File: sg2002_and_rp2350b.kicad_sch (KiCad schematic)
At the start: 33 parts, among them J2 Conn_01x14, J3 Conn_01x14, U10 W25Q128JVSIQTR, X3 12MHz

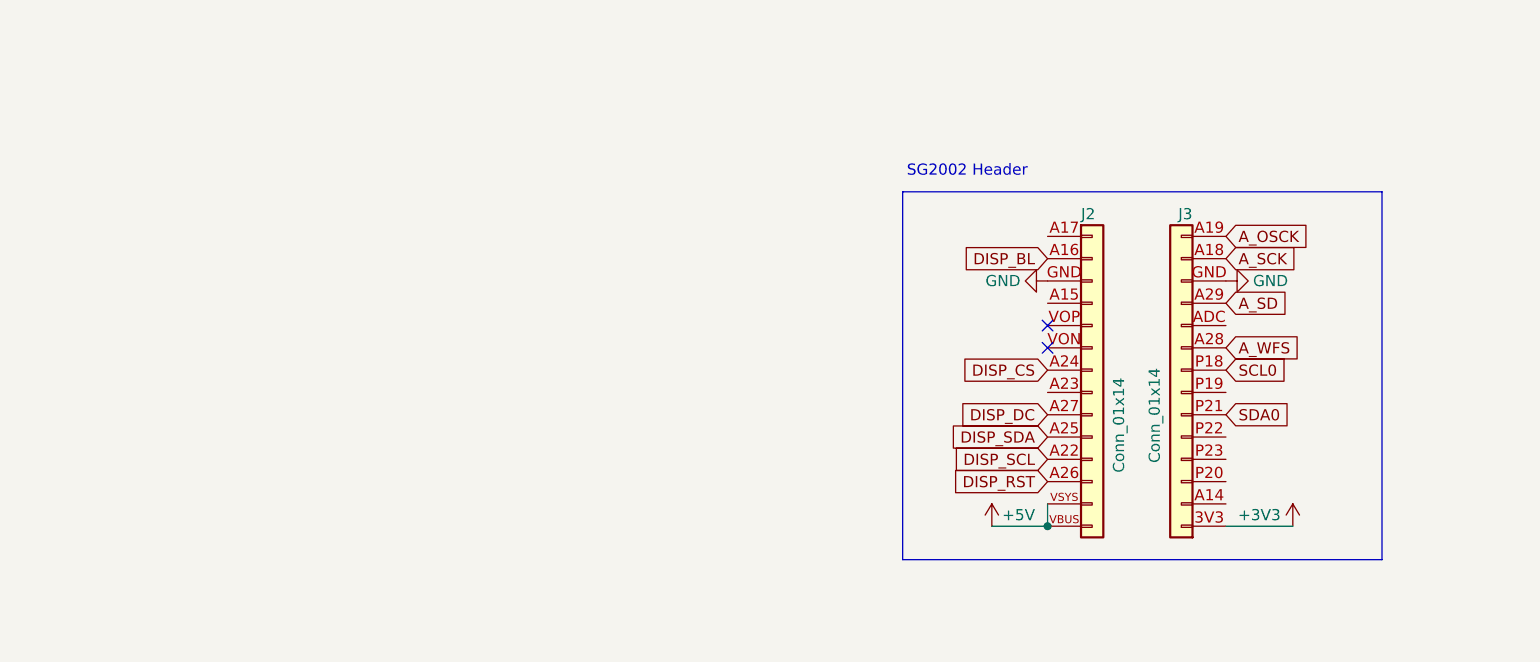
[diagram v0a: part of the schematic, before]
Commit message: Changed to touchscreen LCD and added connectors for front breakout
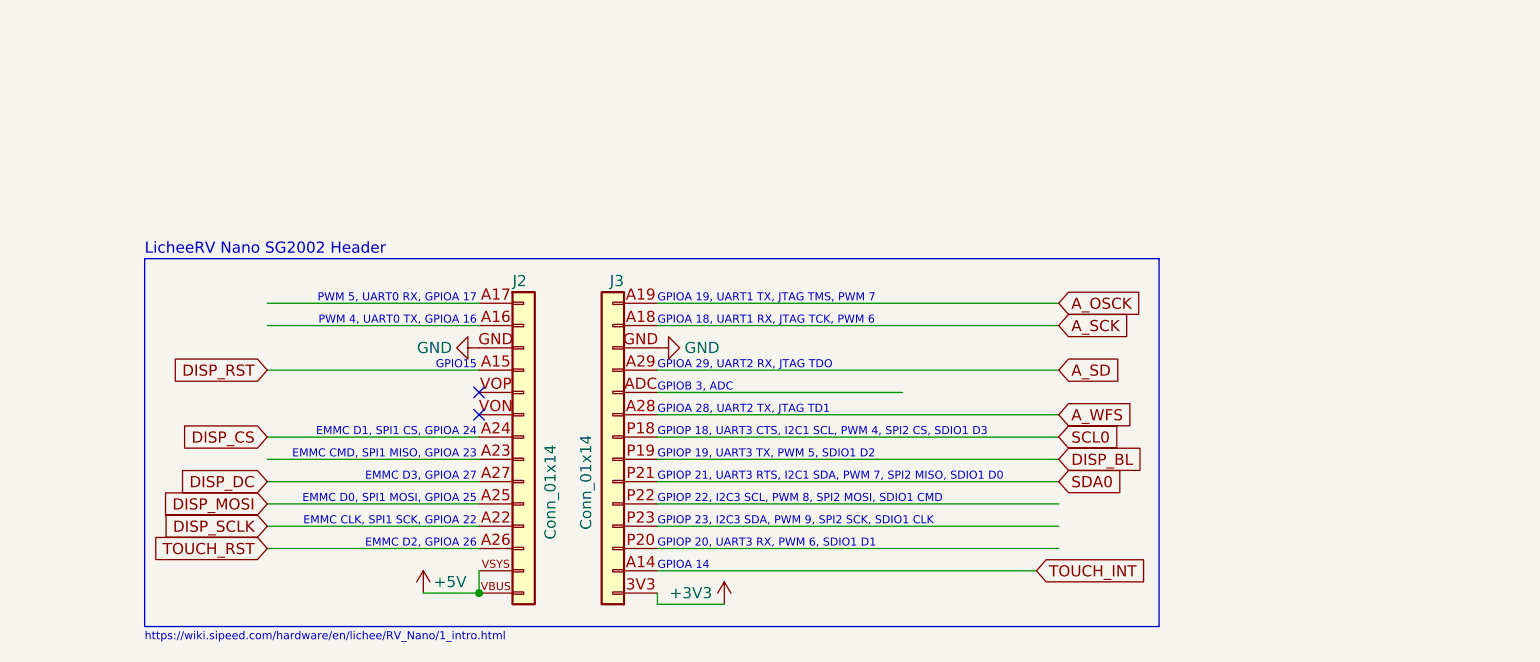
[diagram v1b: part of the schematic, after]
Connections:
- net DISP_BL: now also J3.P19 (Pin_7); no longer J2.A16 (Pin_2)
- net DISP_RST: now also J2.A15 (Pin_4); no longer J2.A26 (Pin_12)
- net TOUCH_INT: now reaches J3.A14 (Pin_2)
- net DISP_SCL renamed DISP_SCLK
- net DISP_SDA renamed DISP_MOSI
- new net TOUCH_RST: J2.A26 (Pin_12)
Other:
- note added: "EMMC CLK, SPI1 SCK, GPIOA 22"
- note added: "EMMC CMD, SPI1 MISO, GPIOA 23"
- note added: "EMMC D0, SPI1 MOSI, GPIOA 25"
- note added: "EMMC D1, SPI1 CS, GPIOA 24"
- note added: "EMMC D2, GPIOA 26"
- note added: "EMMC D3, GPIOA 27"
- note added: "GPIO15"
- note added: "GPIOA 14"
- note added: "GPIOA 18, UART1 RX, JTAG TCK, PWM 6"
- note added: "GPIOA 19, UART1 TX, JTAG TMS, PWM 7"
- note added: "GPIOA 28, UART2 TX, JTAG TD1"
- note added: "GPIOA 29, UART2 RX, JTAG TDO"
- note added: "GPIOB 3, ADC"
- note added: "GPIOP 18, UART3 CTS, I2C1 SCL, PWM 4, SPI2 CS, SDIO1 D3"
- note added: "GPIOP 19, UART3 TX, PWM 5, SDIO1 D2"
- note added: "GPIOP 20, UART3 RX, PWM 6, SDIO1 D1"
- note added: "GPIOP 21, UART3 RTS, I2C1 SDA, PWM 7, SPI2 MISO, SDIO1 D0"
- note added: "GPIOP 22, I2C3 SCL, PWM 8, SPI2 MOSI, SDIO1 CMD"
- note added: "GPIOP 23, I2C3 SDA, PWM 9, SPI2 SCK, SDIO1 CLK"
- note added: "LicheeRV Nano SG2002 Header"
- note added: "PWM 4, UART0 TX, GPIOA 16"
- note added: "PWM 5, UART0 RX, GPIOA 17"
- note added: "https://wiki.sipeed.com/hardware/en/lichee/RV_Nano/1_intro.html"
- note removed: "SG2002 Header"
- moved on the sheet: J2, J3
